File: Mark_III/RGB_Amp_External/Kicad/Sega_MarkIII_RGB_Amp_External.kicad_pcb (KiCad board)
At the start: 2 copper layers, 52 x 57 mm, 17 parts, among them IC1 THS7314D, J1 RGBS Input, J2 VGA Out, J3 Audio, J4 Video Out

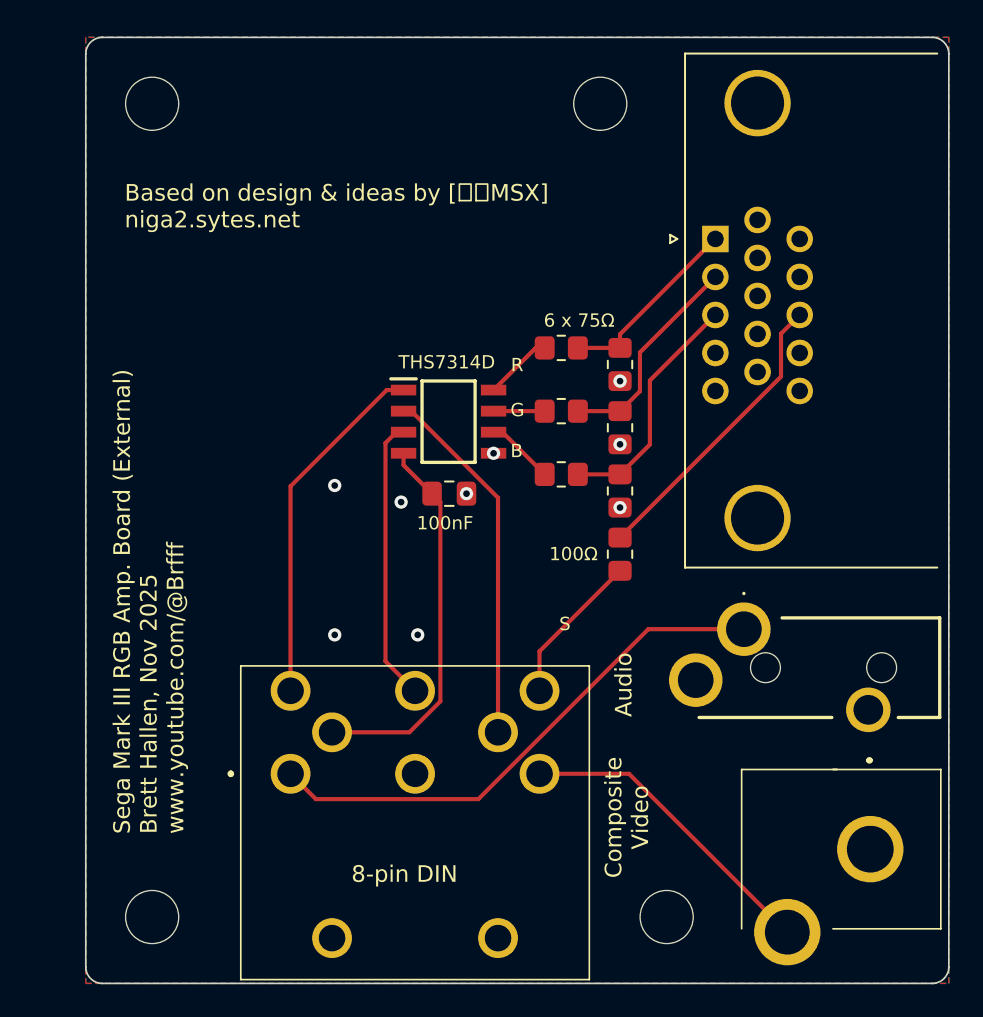
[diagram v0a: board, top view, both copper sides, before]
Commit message: Redesign PCB shape
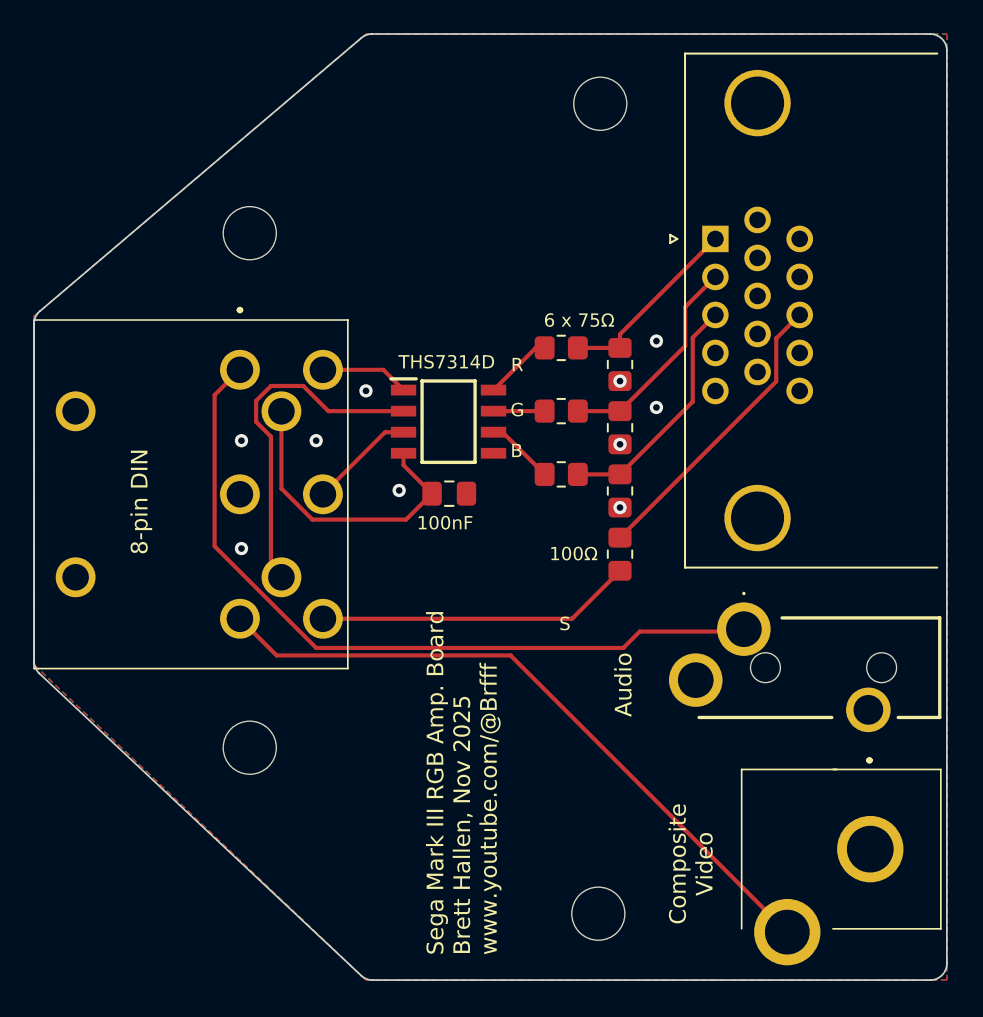
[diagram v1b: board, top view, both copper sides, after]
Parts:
- moved J1 24.5 mm to (89.5, 52.6), turned to 90 degrees
- moved H3 11.8 mm to (90.1, 75.4)
- moved H2 9.77 mm to (90.1, 44.4)
- moved H4 4.12 mm to (111.1, 85.4)
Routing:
- net VIDEO: track 18.9 -> 40.8 mm
- net RED_{IN}: track 21.5 -> 5.36 mm
- net AUDIO: track 32.2 -> 46.2 mm
- net BLUE_{IN}: track 17.0 -> 6.41 mm
- net C.SYNC_{IN}: track 9.24 -> 19.1 mm
- net +5V: track 23.2 -> 18.3 mm
- net GREEN_{IN}: track 22.0 -> 21.1 mm
- net GND: vias 9 -> 10
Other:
- board size 52 x 57 mm -> 55 x 57 mm
- board text added: "Sega Mark III RGB Amp. Board Brett Hallen, Nov 2025 www.youtube.com/@Brfff"
- board text removed: "Sega Mark III RGB Amp. Board (External) Brett Hallen, Nov 2025 www.youtube.com/@Brfff"
